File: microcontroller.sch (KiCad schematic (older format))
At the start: 6 parts

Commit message: Add autoupdated files
Guess we need this....
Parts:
- C? (x3): symbol dmpro-rescue:C -> Effect-Box-rescue:C-dmpro-rescue
- J?: symbol dmpro-rescue:Conn_ARM_JTAG_SWD_20 -> Effect-Box-rescue:Conn_ARM_JTAG_SWD_20-dmpro-rescue
- U?: symbol dmpro-rescue:EFM32GG942F1024 -> Effect-Box-rescue:EFM32GG942F1024-dmpro-rescue
- Y?: symbol dmpro-rescue:Crystal_GND24 -> Effect-Box-rescue:Crystal_GND24-dmpro-rescue
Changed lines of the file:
@@
 EESchema Schematic File Version 4
 LIBS:Effect-Box-cache
-LIBS:dmpro-cache
-LIBS:dmpro2-cache
 EELAYER 30 0
 EELAYER END
@@
 $EndDescr
 $Comp
-L dmpro-rescue:EFM32GG942F1024 U?
+L Effect-Box-rescue:EFM32GG942F1024-dmpro-rescue U?
 U 1 1 5D7F7450
 P 4450 2250
+AR Path="/5D7F7450" Ref="U?"  Part="1"
+AR Path="/5D7D441F/5D7F7450" Ref="U?"  Part="1"
 F 0 "U?" H 5550 2650 60  0000 C CNN
 F 1 "EFM32GG942F1024" H 5550 2550 60  0000 C CNN
@@
 $EndComp
 $Comp
-L dmpro-rescue:GND #PWR?
+L Effect-Box-rescue:GND-dmpro-rescue #PWR?
 U 1 1 5D7F8673
 P 3150 2950
+AR Path="/5D7F8673" Ref="#PWR?"  Part="1"
+AR Path="/5D7D441F/5D7F8673" Ref="#PWR?"  Part="1"
 F 0 "#PWR?" H 3150 2700 50  0001 C CNN
 F 1 "GND" H 3150 2800 50  0000 C CNN
@@
 	8750 3300 8750 3750
 $Comp
-L dmpro-rescue:GND #PWR?
+L Effect-Box-rescue:GND-dmpro-rescue #PWR?
 U 1 1 5D7F97BF
 P 10050 4200
+AR Path="/5D7F97BF" Ref="#PWR?"  Part="1"
+AR Path="/5D7D441F/5D7F97BF" Ref="#PWR?"  Part="1"
 F 0 "#PWR?" H 10050 3950 50  0001 C CNN
 F 1 "GND" H 10050 4050 50  0000 C CNN
@@
 $EndComp
 $Comp
-L dmpro-rescue:Conn_ARM_JTAG_SWD_20 J?
+L Effect-Box-rescue:Conn_ARM_JTAG_SWD_20-dmpro-rescue J?
 U 1 1 5D7F9345
 P 9950 3400
+AR Path="/5D7F9345" Ref="J?"  Part="1"
+AR Path="/5D7D441F/5D7F9345" Ref="J?"  Part="1"
 F 0 "J?" H 9750 4250 50  0000 R CNN
 F 1 "Conn_ARM_JTAG_SWD_20" H 9750 4150 50  0000 R BNN
@@
 $EndComp
 $Comp
-L dmpro-rescue:C C?
+L Effect-Box-rescue:C-dmpro-rescue C?
 U 1 1 5D7F90BC
 P 2600 6550
+AR Path="/5D7F90BC" Ref="C?"  Part="1"
+AR Path="/5D7D441F/5D7F90BC" Ref="C?"  Part="1"
 F 0 "C?" H 2625 6650 50  0000 L CNN
 F 1 "C" H 2625 6450 50  0000 L CNN
@@
 $EndComp
 $Comp
-L dmpro-rescue:C C?
+L Effect-Box-rescue:C-dmpro-rescue C?
 U 1 1 5D7F908A
 P 1600 6550
+AR Path="/5D7F908A" Ref="C?"  Part="1"
+AR Path="/5D7D441F/5D7F908A" Ref="C?"  Part="1"
 F 0 "C?" H 1625 6650 50  0000 L CNN
 F 1 "C" H 1625 6450 50  0000 L CNN
@@
 $EndComp
 $Comp
-L dmpro-rescue:GND #PWR?
+L Effect-Box-rescue:GND-dmpro-rescue #PWR?
 U 1 1 5D7F9042
 P 2100 6800
+AR Path="/5D7F9042" Ref="#PWR?"  Part="1"
+AR Path="/5D7D441F/5D7F9042" Ref="#PWR?"  Part="1"
 F 0 "#PWR?" H 2100 6550 50  0001 C CNN
 F 1 "GND" H 2100 6650 50  0000 C CNN
@@
 $EndComp
 $Comp
-L dmpro-rescue:GND #PWR?
+L Effect-Box-rescue:GND-dmpro-rescue #PWR?
 U 1 1 5D7F8FCF
 P 1900 5500
+AR Path="/5D7F8FCF" Ref="#PWR?"  Part="1"
+AR Path="/5D7D441F/5D7F8FCF" Ref="#PWR?"  Part="1"
 F 0 "#PWR?" H 1900 5250 50  0001 C CNN
 F 1 "GND" H 1900 5350 50  0000 C CNN
@@
 $EndComp
 $Comp
-L dmpro-rescue:Crystal_GND24 Y?
+L Effect-Box-rescue:Crystal_GND24-dmpro-rescue Y?
 U 1 1 5D7F8E7E
 P 2100 6100
+AR Path="/5D7F8E7E" Ref="Y?"  Part="1"
+AR Path="/5D7D441F/5D7F8E7E" Ref="Y?"  Part="1"
 F 0 "Y?" H 2225 6300 50  0000 L CNN
 F 1 "Crystal_GND24" H 2225 6225 50  0000 L CNN
@@
 $EndComp
 $Comp
-L dmpro-rescue:GND #PWR?
+L Effect-Box-rescue:GND-dmpro-rescue #PWR?
 U 1 1 5D7F8D54
 P 7800 4500
+AR Path="/5D7F8D54" Ref="#PWR?"  Part="1"
+AR Path="/5D7D441F/5D7F8D54" Ref="#PWR?"  Part="1"
 F 0 "#PWR?" H 7800 4250 50  0001 C CNN
 F 1 "GND" H 7800 4350 50  0000 C CNN
@@
 $EndComp
 $Comp
-L dmpro-rescue:C C?
+L Effect-Box-rescue:C-dmpro-rescue C?
 U 1 1 5D7F8CED
 P 7800 4350
+AR Path="/5D7F8CED" Ref="C?"  Part="1"
+AR Path="/5D7D441F/5D7F8CED" Ref="C?"  Part="1"
 F 0 "C?" H 7825 4450 50  0000 L CNN
 F 1 "C" H 7825 4250 50  0000 L CNN
@@
 $EndComp
 $Comp
-L dmpro-rescue:+3.3V #PWR?
+L Effect-Box-rescue:+3.3V-dmpro-rescue #PWR?
 U 1 1 5D7F877D
 P 5450 1300
+AR Path="/5D7F877D" Ref="#PWR?"  Part="1"
+AR Path="/5D7D441F/5D7F877D" Ref="#PWR?"  Part="1"
 F 0 "#PWR?" H 5450 1150 50  0001 C CNN
 F 1 "+3.3V" H 5450 1440 50  0000 C CNN
@@
 $EndComp
 $Comp
-L dmpro-rescue:GND #PWR?
+L Effect-Box-rescue:GND-dmpro-rescue #PWR?
 U 1 1 5D7F8568
 P 7800 3050
+AR Path="/5D7F8568" Ref="#PWR?"  Part="1"
+AR Path="/5D7D441F/5D7F8568" Ref="#PWR?"  Part="1"
 F 0 "#PWR?" H 7800 2800 50  0001 C CNN
 F 1 "GND" H 7800 2900 50  0000 C CNN

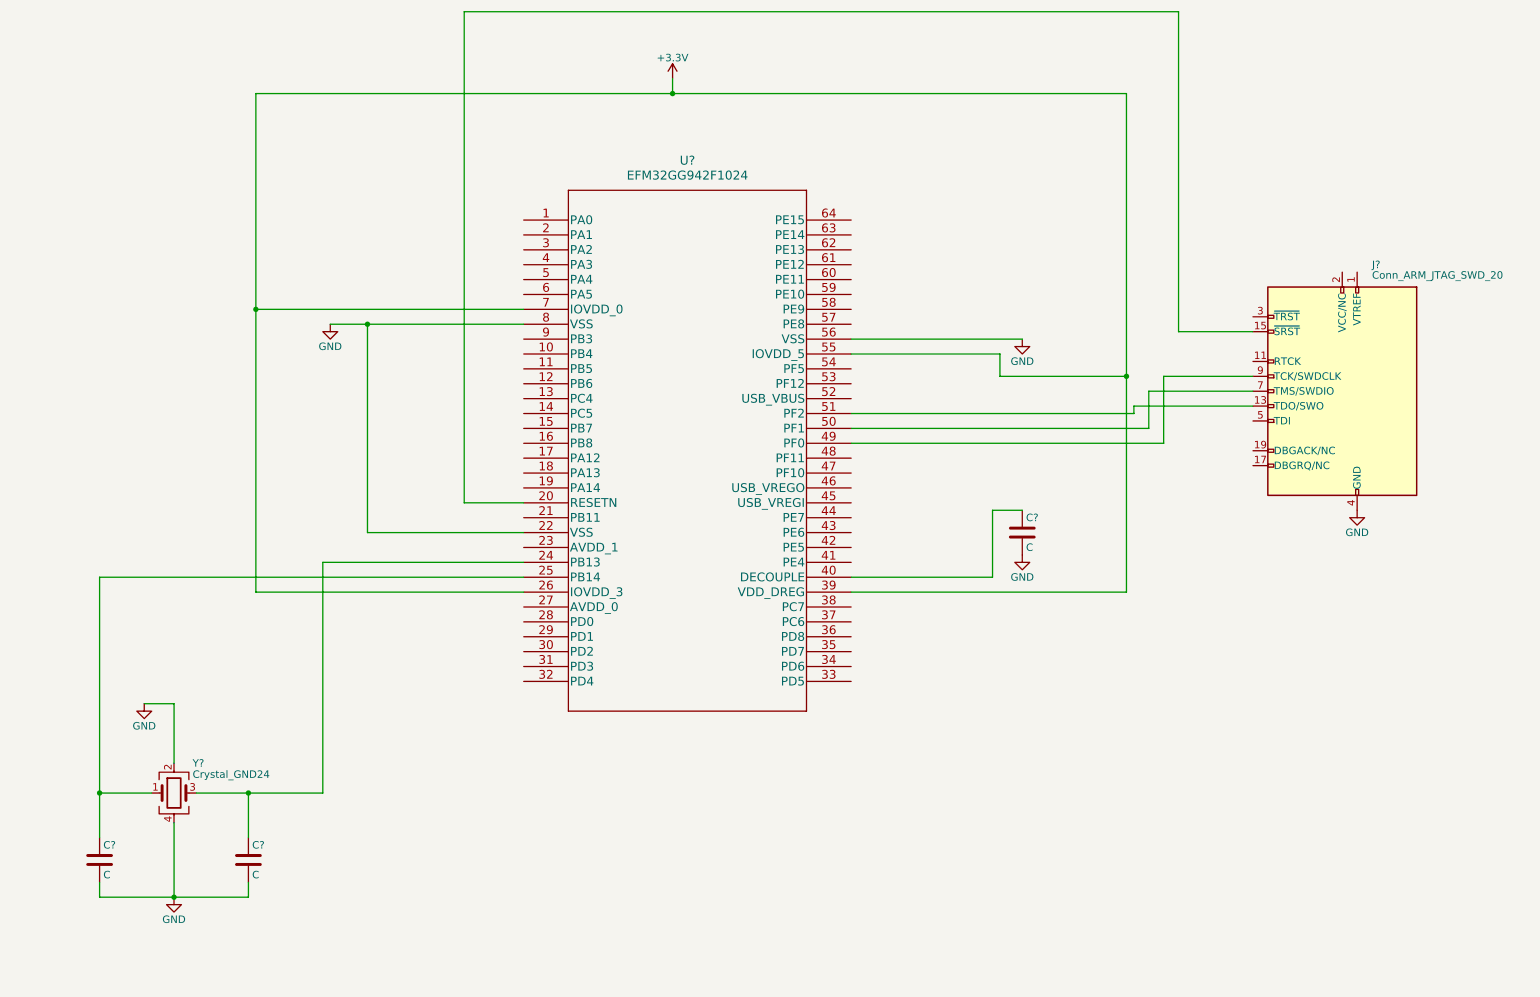
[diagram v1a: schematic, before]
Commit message: Add capacitors
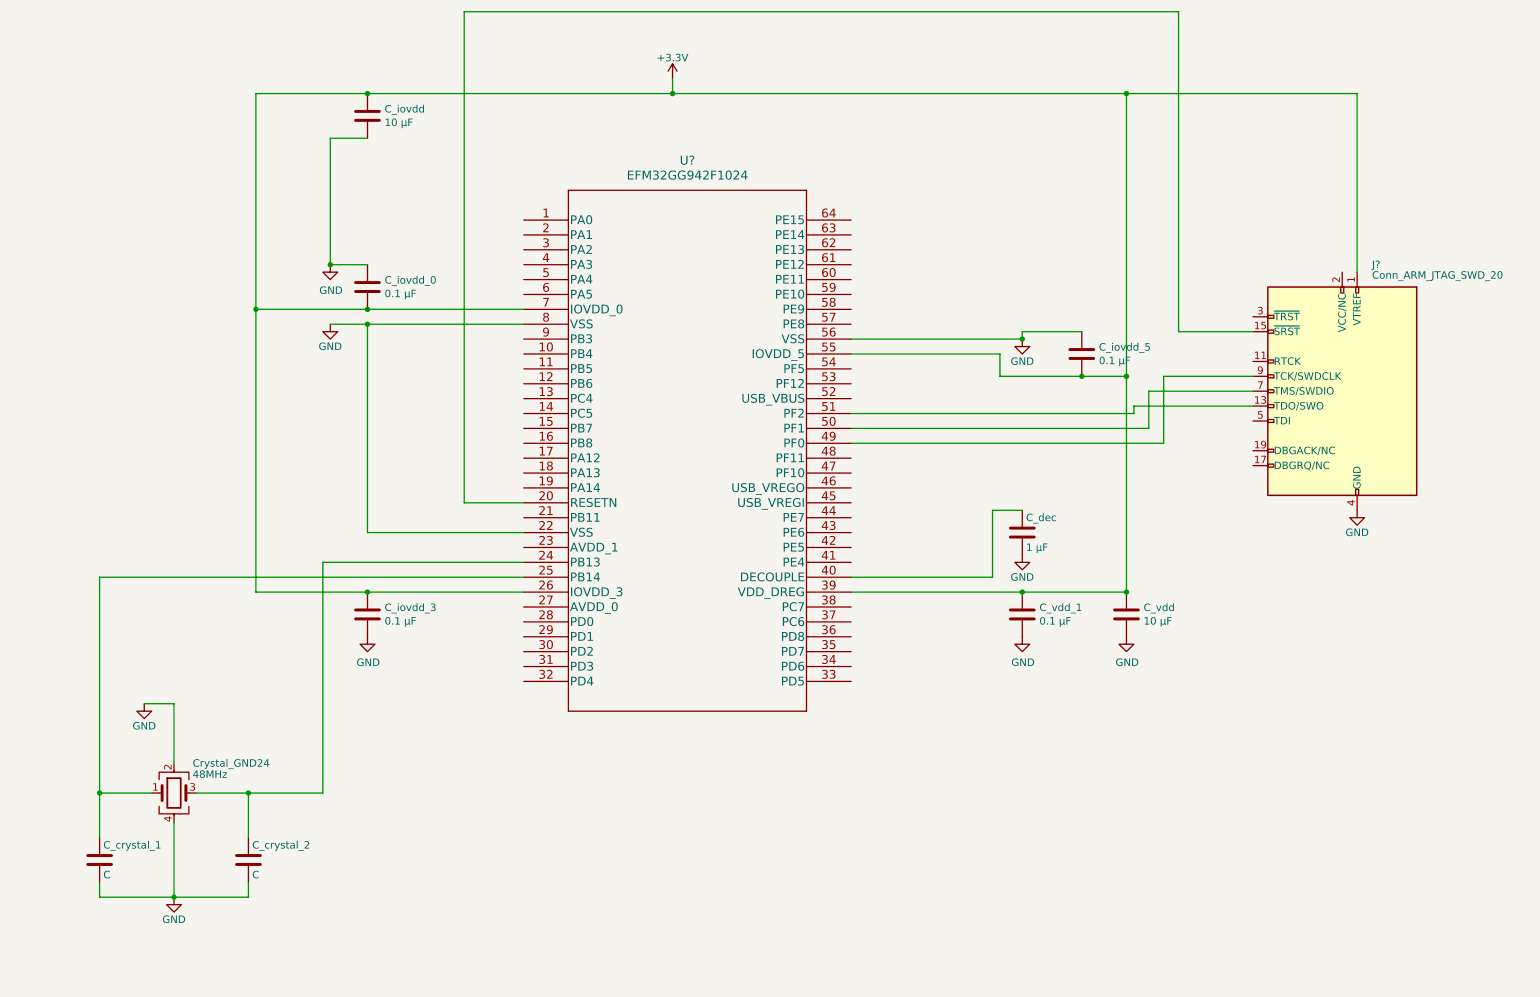
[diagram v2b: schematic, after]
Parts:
- added C_iovdd, C_vdd: 10 µF, symbol Device:C
- added C_iovdd_0, C_iovdd_3, C_iovdd_5, C_vdd_1: 0.1 µF, symbol Device:C
- C_dec: renamed from C?; value C -> 1 µF
- Crystal_GND24: renamed from Y?; value Crystal_GND24 -> 48MHz
- gave numbers to parts that had none: 2
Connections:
- net +3V3: now also J?.1 (VTREF), C_iovdd.1, C_iovdd_0.2, C_iovdd_3.1, C_iovdd_5.2, C_vdd.1, C_vdd_1.1
- net GND: now also C_iovdd.2, C_iovdd_0.1, C_iovdd_3.2, C_iovdd_5.1, C_vdd.2, C_vdd_1.2
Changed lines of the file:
@@
 $EndComp
 $Comp
-L Effect-Box-rescue:GND-dmpro-rescue #PWR?
+L Effect-Box-rescue:GND-dmpro-rescue #PWR0112
 U 1 1 5D7F8673
 P 3150 2950
-AR Path="/5D7F8673" Ref="#PWR?"  Part="1"
-AR Path="/5D7D441F/5D7F8673" Ref="#PWR?"  Part="1"
-F 0 "#PWR?" H 3150 2700 50  0001 C CNN
+F 0 "#PWR0112" H 3150 2700 50  0001 C CNN
 F 1 "GND" H 3150 2800 50  0000 C CNN
 F 2 "" H 3150 2950 50  0001 C CNN
@@
 	6650 4650 7600 4650
 Wire Wire Line
-	2650 4750 4450 4750
+	2650 4750 3400 4750
 Wire Wire Line
 	6650 3150 7650 3150
 Wire Wire Line
-	6650 4750 8500 4750
-Wire Wire Line
-	4450 2850 2650 2850
+	6650 4750 7800 4750
+Wire Wire Line
+	4450 2850 3400 2850
 Connection ~ 3400 2950
 Wire Wire Line
@@
 	2650 2850 2650 4750
 Wire Wire Line
-	5450 1400 2650 1400
+	5450 1400 3400 1400
 Wire Wire Line
 	8500 3300 8500 1400
@@
 	7650 3150 7650 3300
 Wire Wire Line
-	7650 3300 8500 3300
+	7650 3300 8200 3300
 Connection ~ 8500 3300
 Wire Wire Line
@@
 	8750 3300 8750 3750
 $Comp
-L Effect-Box-rescue:GND-dmpro-rescue #PWR?
+L Effect-Box-rescue:GND-dmpro-rescue #PWR0113
 U 1 1 5D7F97BF
 P 10050 4200
-AR Path="/5D7F97BF" Ref="#PWR?"  Part="1"
-AR Path="/5D7D441F/5D7F97BF" Ref="#PWR?"  Part="1"
-F 0 "#PWR?" H 10050 3950 50  0001 C CNN
+F 0 "#PWR0113" H 10050 3950 50  0001 C CNN
 F 1 "GND" H 10050 4050 50  0000 C CNN
 F 2 "" H 10050 4200 50  0001 C CNN
@@
 $EndComp
 $Comp
-L Effect-Box-rescue:C-dmpro-rescue C?
+L Effect-Box-rescue:C-dmpro-rescue C_crystal_2
 U 1 1 5D7F90BC
 P 2600 6550
-AR Path="/5D7F90BC" Ref="C?"  Part="1"
-AR Path="/5D7D441F/5D7F90BC" Ref="C?"  Part="1"
-F 0 "C?" H 2625 6650 50  0000 L CNN
+F 0 "C_crystal_2" H 2625 6650 50  0000 L CNN
 F 1 "C" H 2625 6450 50  0000 L CNN
 F 2 "" H 2638 6400 50  0001 C CNN
@@
 $EndComp
 $Comp
-L Effect-Box-rescue:C-dmpro-rescue C?
+L Effect-Box-rescue:C-dmpro-rescue C_crystal_1
 U 1 1 5D7F908A
 P 1600 6550
-AR Path="/5D7F908A" Ref="C?"  Part="1"
-AR Path="/5D7D441F/5D7F908A" Ref="C?"  Part="1"
-F 0 "C?" H 1625 6650 50  0000 L CNN
+F 0 "C_crystal_1" H 1625 6650 50  0000 L CNN
 F 1 "C" H 1625 6450 50  0000 L CNN
 F 2 "" H 1638 6400 50  0001 C CNN
@@
 $EndComp
 $Comp
-L Effect-Box-rescue:GND-dmpro-rescue #PWR?
+L Effect-Box-rescue:GND-dmpro-rescue #PWR0114
 U 1 1 5D7F9042
 P 2100 6800
-AR Path="/5D7F9042" Ref="#PWR?"  Part="1"
-AR Path="/5D7D441F/5D7F9042" Ref="#PWR?"  Part="1"
-F 0 "#PWR?" H 2100 6550 50  0001 C CNN
+F 0 "#PWR0114" H 2100 6550 50  0001 C CNN
 F 1 "GND" H 2100 6650 50  0000 C CNN
 F 2 "" H 2100 6800 50  0001 C CNN
@@
 $EndComp
 $Comp
-L Effect-Box-rescue:GND-dmpro-rescue #PWR?
+L Effect-Box-rescue:GND-dmpro-rescue #PWR0115
 U 1 1 5D7F8FCF
 P 1900 5500
-AR Path="/5D7F8FCF" Ref="#PWR?"  Part="1"
-AR Path="/5D7D441F/5D7F8FCF" Ref="#PWR?"  Part="1"
-F 0 "#PWR?" H 1900 5250 50  0001 C CNN
+F 0 "#PWR0115" H 1900 5250 50  0001 C CNN
 F 1 "GND" H 1900 5350 50  0000 C CNN
 F 2 "" H 1900 5500 50  0001 C CNN
@@
 $EndComp
 $Comp
-L Effect-Box-rescue:Crystal_GND24-dmpro-rescue Y?
+L Effect-Box-rescue:Crystal_GND24-dmpro-rescue Crystal_GND24
 U 1 1 5D7F8E7E
 P 2100 6100
-AR Path="/5D7F8E7E" Ref="Y?"  Part="1"
-AR Path="/5D7D441F/5D7F8E7E" Ref="Y?"  Part="1"
-F 0 "Y?" H 2225 6300 50  0000 L CNN
-F 1 "Crystal_GND24" H 2225 6225 50  0000 L CNN
+F 0 "Crystal_GND24" H 2225 6300 50  0000 L CNN
+F 1 "48MHz" H 2225 6225 50  0000 L CNN
 F 2 "" H 2100 6100 50  0001 C CNN
 F 3 "" H 2100 6100 50  0001 C CNN
@@
 $EndComp
 $Comp
-L Effect-Box-rescue:GND-dmpro-rescue #PWR?
+L Effect-Box-rescue:GND-dmpro-rescue #PWR0116
 U 1 1 5D7F8D54
 P 7800 4500
-AR Path="/5D7F8D54" Ref="#PWR?"  Part="1"
-AR Path="/5D7D441F/5D7F8D54" Ref="#PWR?"  Part="1"
-F 0 "#PWR?" H 7800 4250 50  0001 C CNN
+F 0 "#PWR0116" H 7800 4250 50  0001 C CNN
 F 1 "GND" H 7800 4350 50  0000 C CNN
 F 2 "" H 7800 4500 50  0001 C CNN
@@
 $EndComp
 $Comp
-L Effect-Box-rescue:C-dmpro-rescue C?
+L Effect-Box-rescue:C-dmpro-rescue C_dec
 U 1 1 5D7F8CED
 P 7800 4350
-AR Path="/5D7F8CED" Ref="C?"  Part="1"
-AR Path="/5D7D441F/5D7F8CED" Ref="C?"  Part="1"
-F 0 "C?" H 7825 4450 50  0000 L CNN
-F 1 "C" H 7825 4250 50  0000 L CNN
+F 0 "C_dec" H 7825 4450 50  0000 L CNN
+F 1 "1 µF" H 7825 4250 50  0000 L CNN
 F 2 "" H 7838 4200 50  0001 C CNN
 F 3 "" H 7800 4350 50  0001 C CNN
@@
 $EndComp
 $Comp
-L Effect-Box-rescue:+3.3V-dmpro-rescue #PWR?
+L Effect-Box-rescue:+3.3V-dmpro-rescue #PWR0117
 U 1 1 5D7F877D
 P 5450 1300
-AR Path="/5D7F877D" Ref="#PWR?"  Part="1"
-AR Path="/5D7D441F/5D7F877D" Ref="#PWR?"  Part="1"
-F 0 "#PWR?" H 5450 1150 50  0001 C CNN
+F 0 "#PWR0117" H 5450 1150 50  0001 C CNN
 F 1 "+3.3V" H 5450 1440 50  0000 C CNN
 F 2 "" H 5450 1300 50  0001 C CNN
@@
 $EndComp
 $Comp
-L Effect-Box-rescue:GND-dmpro-rescue #PWR?
+L Effect-Box-rescue:GND-dmpro-rescue #PWR0118
 U 1 1 5D7F8568
 P 7800 3050
-AR Path="/5D7F8568" Ref="#PWR?"  Part="1"
-AR Path="/5D7D441F/5D7F8568" Ref="#PWR?"  Part="1"
-F 0 "#PWR?" H 7800 2800 50  0001 C CNN
+F 0 "#PWR0118" H 7800 2800 50  0001 C CNN
 F 1 "GND" H 7800 2900 50  0000 C CNN
 F 2 "" H 7800 3050 50  0001 C CNN
@@
 	1    0    0    -1
 $EndComp
+Wire Wire Line
+	10050 2600 10050 1400
+Wire Wire Line
+	10050 1400 8500 1400
+Connection ~ 8500 1400
+$Comp
+L Device:C C_vdd_1
+U 1 1 5D810379
+P 7800 4900
+F 0 "C_vdd_1" H 7915 4946 50  0000 L CNN
+F 1 "0.1 µF" H 7915 4855 50  0000 L CNN
+F 2 "" H 7838 4750 50  0001 C CNN
+F 3 "~" H 7800 4900 50  0001 C CNN
+	1    7800 4900
+	1    0    0    -1
+$EndComp
+Connection ~ 7800 4750
+Wire Wire Line
+	7800 4750 8500 4750
+$Comp
+L power:GND #PWR?
+U 1 1 5D811F79
+P 7800 5050
+F 0 "#PWR?" H 7800 4800 50  0001 C CNN
+F 1 "GND" H 7805 4877 50  0000 C CNN
+F 2 "" H 7800 5050 50  0001 C CNN
+F 3 "" H 7800 5050 50  0001 C CNN
+	1    7800 5050
+	1    0    0    -1
+$EndComp
+$Comp
+L Device:C C_vdd
+U 1 1 5D8125F5
+P 8500 4900
+F 0 "C_vdd" H 8615 4946 50  0000 L CNN
+F 1 "10 µF" H 8615 4855 50  0000 L CNN
+F 2 "" H 8538 4750 50  0001 C CNN
+F 3 "~" H 8500 4900 50  0001 C CNN
+	1    8500 4900
+	1    0    0    -1
+$EndComp
+Connection ~ 8500 4750
+$Comp
+L power:GND #PWR?
+U 1 1 5D813461
+P 8500 5050
+F 0 "#PWR?" H 8500 4800 50  0001 C CNN
+F 1 "GND" H 8505 4877 50  0000 C CNN
+F 2 "" H 8500 5050 50  0001 C CNN
+F 3 "" H 8500 5050 50  0001 C CNN
+	1    8500 5050
+	1    0    0    -1
+$EndComp
+$Comp
+L Device:C C_iovdd_3
+U 1 1 5D8144C8
+P 3400 4900
+F 0 "C_iovdd_3" H 3515 4946 50  0000 L CNN
+F 1 "0.1 µF" H 3515 4855 50  0000 L CNN
+F 2 "" H 3438 4750 50  0001 C CNN
+F 3 "~" H 3400 4900 50  0001 C CNN
+	1    3400 4900
+	1    0    0    -1
+$EndComp
+Connection ~ 3400 4750
+Wire Wire Line
+	3400 4750 4450 4750
+$Comp
+L power:GND #PWR?
+U 1 1 5D814E43
+P 3400 5050
+F 0 "#PWR?" H 3400 4800 50  0001 C CNN
+F 1 "GND" H 3405 4877 50  0000 C CNN
+F 2 "" H 3400 5050 50  0001 C CNN
+F 3 "" H 3400 5050 50  0001 C CNN
+	1    3400 5050
+	1    0    0    -1
+$EndComp
+$Comp
+L Device:C C_iovdd_0
+U 1 1 5D8162EF
+P 3400 2700
+F 0 "C_iovdd_0" H 3515 2746 50  0000 L CNN
+F 1 "0.1 µF" H 3515 2655 50  0000 L CNN
+F 2 "" H 3438 2550 50  0001 C CNN
+F 3 "~" H 3400 2700 50  0001 C CNN
+	1    3400 2700
+	1    0    0    -1
+$EndComp
+Connection ~ 3400 2850
+Wire Wire Line
+	3400 2850 2650 2850
+$Comp
+L power:GND #PWR?
+U 1 1 5D81A071
+P 3150 2550
+F 0 "#PWR?" H 3150 2300 50  0001 C CNN
+F 1 "GND" H 3155 2377 50  0000 C CNN
+F 2 "" H 3150 2550 50  0001 C CNN
+F 3 "" H 3150 2550 50  0001 C CNN
+	1    3150 2550
+	1    0    0    -1
+$EndComp
+Wire Wire Line
+	3400 2550 3150 2550
+$Comp
+L Device:C C_iovdd_5
+U 1 1 5D81BBBF
+P 8200 3150
+F 0 "C_iovdd_5" H 8315 3196 50  0000 L CNN
+F 1 "0.1 µF" H 8315 3105 50  0000 L CNN
+F 2 "" H 8238 3000 50  0001 C CNN
+F 3 "~" H 8200 3150 50  0001 C CNN
+	1    8200 3150
+	1    0    0    -1
+$EndComp
+Connection ~ 8200 3300
+Wire Wire Line
+	8200 3300 8500 3300
+Wire Wire Line
+	8200 3000 7800 3000
+Wire Wire Line
+	7800 3000 7800 3050
+Connection ~ 7800 3050
+$Comp
+L Device:C C_iovdd
+U 1 1 5D820429
+P 3400 1550
+F 0 "C_iovdd" H 3515 1596 50  0000 L CNN
+F 1 "10 µF" H 3515 1505 50  0000 L CNN
+F 2 "" H 3438 1400 50  0001 C CNN
+F 3 "~" H 3400 1550 50  0001 C CNN
+	1    3400 1550
+	1    0    0    -1
+$EndComp
+Connection ~ 3400 1400
+Wire Wire Line
+	3400 1400 2650 1400
+Wire Wire Line
+	3400 1700 3150 1700
+Wire Wire Line
+	3150 1700 3150 2550
+Connection ~ 3150 2550
 $EndSCHEMATC
